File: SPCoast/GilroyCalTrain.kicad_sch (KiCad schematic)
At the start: 94 parts, among them SW3771 771, SW3773 773, SW3775 775

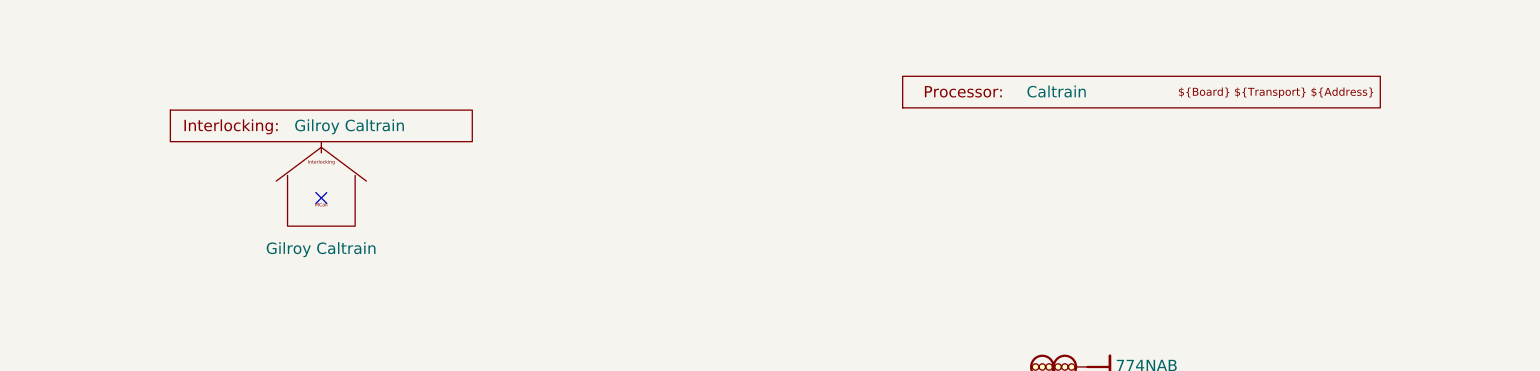
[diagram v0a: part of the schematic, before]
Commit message: chore(kicad): owner mockup: explicit seam wiring on Luchessa and South-cTc, host and bus pins
Owner's edits, committed as they stand (2026-10-21), before scripted edits build on them.

- Interlocking gains Codeline and Host pins; MAIN HOUSE's Interlocking pin is Codeline.
- OfficeUnit gains Host and Codeline pins; JohnCTC desk processor drawn on South-cTc.
- Processor gains Transport and IO pins; MAX7313 and MCP23017 gain an I2C bus pin.
- Transports: Codeline pin renamed Host; JMRI_MQTT instance added; Loconet removed.
- Encodings' pin renamed Transport; Luchessa's 506 and Bit Packing instances removed.
- SPCoastApp virtual host (FieldUnit_Virtual) hosts CMRInet and JMRI_MQTT.
- Luchessa: unit, houses and Time Coded on one net; Host to its own processor;
  panel MAX7313s on the desk bus (OfficeBus).
- Watsonville, Caltrain, Interchange: first-pass Processor placeholders, to be redrawn.

Verified: netlist and ERC exported from the saved project; field diff against the
committed netlist shows no per-instance field lost.
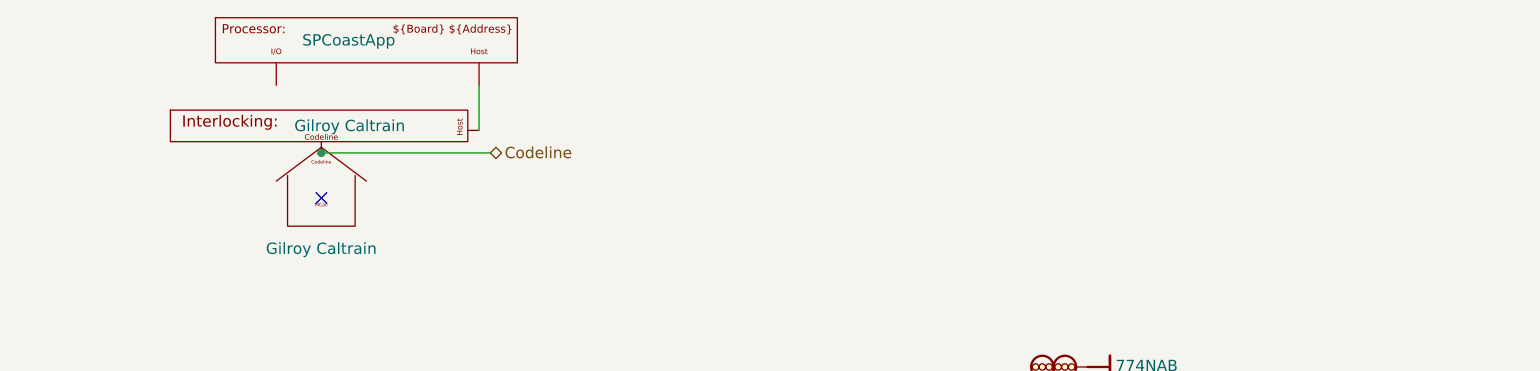
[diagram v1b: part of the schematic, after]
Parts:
- Proc1: value Caltrain -> SPCoastApp
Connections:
- net Codeline: now reaches HOUSE3001.2 (Codeline), Plant3001.1 (Codeline)
- new net: Plant3001.2 (Host), Proc1.1 (Transport)
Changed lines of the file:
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@@
 	)
 	(junction
+		(at 69.85 29.21)
+		(diameter 0)
+		(color 0 0 0 0)
+	)
+	(junction
 		(at 58.42 59.69)
 		(diameter 0)
@@
 	(wire
 		(pts
+			(xy 87.63 21.59) (xy 87.63 26.67)
+		)
+		(stroke
+			(width 0)
+			(type default)
+		)
+	)
+	(wire
+		(pts
 			(xy 125.73 91.44) (xy 110.49 76.2)
 		)
@@
 	(wire
 		(pts
+			(xy 69.85 29.21) (xy 88.9 29.21)
+		)
+		(stroke
+			(width 0)
+			(type default)
+		)
+	)
+	(wire
+		(pts
 			(xy 97.79 165.1) (xy 104.14 165.1)
 		)
@@
 		)
 	)
+	(hierarchical_label "Codeline"
+		(shape bidirectional)
+		(at 88.9 29.21 0)
+		(effects
+			(font
+				(size 1.27 1.27)
+			)
+			(justify left)
+		)
+	)
 	(symbol
 		(lib_id "Railroad-Trackplan:Bumper")
@@
 		(pin "1"
 		)
+		(pin "2"
+		)
 		(instances
 			(project "SPCoast"
@@
 	(symbol
 		(lib_id "Railroad-HardwareIO:Processor")
-		(at 152.4 25.4 0)
+		(at 74.93 16.51 0)
 		(unit 1)
 		(body_style 1)
@@
 		(dnp no)
 		(property "Reference" "Proc1"
-			(at 138.176 19.558 0)
+			(at 60.706 10.668 0)
 			(hide yes)
 			(show_name no)
@@
 			)
 		)
-		(property "Value" "Caltrain"
-			(at 149.352 22.352 0)
+		(property "Value" "SPCoastApp"
+			(at 67.691 16.51 0)
 			(show_name no)
-			(do_not_autoplace no)
+			(do_not_autoplace yes)
 			(effects
 				(font
@@
 		)
 		(property "Footprint" ""
-			(at 152.4 25.4 0)
+			(at 74.93 16.51 0)
 			(hide yes)
 			(show_name no)
@@
 		)
 		(property "Datasheet" ""
-			(at 152.4 25.4 0)
+			(at 74.93 16.51 0)
 			(hide yes)
 			(show_name no)
@@
 		)
 		(property "Description" "A processor: declares the I2C bus and GPIO pins of the chips and drivers in its scope; with Transport and Address it is a node on that code line (ADR 0005)."
-			(at 152.4 25.4 0)
+			(at 76.2 20.32 0)
 			(hide yes)
 			(show_name no)
@@
 		)
 		(property "Role" "STRUCTURE"
-			(at 152.4 25.4 0)
+			(at 63.627 6.858 0)
 			(hide yes)
 			(show_name no)
@@
 		)
 		(property "Kind" "PROCESSOR"
-			(at 152.4 25.4 0)
+			(at 65.024 8.509 0)
 			(hide yes)
 			(show_name no)
@@
 		)
 		(property "Board" "cpNode"
-			(at 152.4 25.4 0)
+			(at 74.93 16.51 0)
 			(hide yes)
 			(show_name no)
@@
 		)
 		(property "Transport" "CMRInet"
-			(at 152.4 25.4 0)
+			(at 74.93 16.51 0)
 			(hide yes)
 			(show_name no)
@@
 		)
 		(property "Address" "30"
-			(at 152.4 25.4 0)
+			(at 74.93 16.51 0)
 			(hide yes)
 			(show_name no)
@@
 			)
 		)
+		(pin "1"
+		)
+		(pin "2"
+		)
 		(instances
